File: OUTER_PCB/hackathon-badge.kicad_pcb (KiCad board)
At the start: 2 copper layers, 97.8 x 87.5 mm, 19 parts

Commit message: finished the outer board
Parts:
- removed the D1 at (154.5, 84.4)
- removed the D10 at (153.5, 128.4)
- removed D15: WS2812B-2020, LED_SMD:LED_WS2812B-2020_PLCC4_2.0x2.0mm
- removed the D5 at (175.7, 103.1)
- added TP1: TestPoint, TestPoint:TestPoint_Pad_4.0x4.0mm, B.Cu at (131.0, 106.0)
- added TP2: TestPoint, TestPoint:TestPoint_Pad_4.0x4.0mm, B.Cu at (177.0, 105.5)
- added TP3: TestPoint, TestPoint:TestPoint_Pad_4.0x4.0mm, B.Cu at (154.0, 84.0)
- added TP4: TestPoint, TestPoint:TestPoint_Pad_4.0x4.0mm, B.Cu at (154.0, 130.0)
- moved G*** 12.5 mm to (153.9, 118.5)
- moved D12 3.64 mm to (134.1, 98.5), turned to -110 degrees
- moved D11 1.37 mm to (133.0, 110.9), turned to -80 degrees
- moved D13 0.93 mm to (140.1, 90.2), turned to -140 degrees
- moved D4 0.87 mm to (174.8, 111.2), turned to 80 degrees
- moved D3 0.85 mm to (172.6, 96.4), turned to 120 degrees
- moved D14 0.84 mm to (146.7, 86.4), turned to -160 degrees
- moved D2 0.83 mm to (167.9, 90.5), turned to 140 degrees
- moved D1 0.80 mm to (161.7, 86.7), turned to 160 degrees
- moved D9 0.69 mm to (139.3, 122.3), turned to -40 degrees
- moved D7 0.60 mm to (160.5, 127.0), turned to 20 degrees
- moved D5 0.58 mm to (172.2, 117.8), turned to 60 degrees
- moved D10 0.55 mm to (135.2, 116.9), turned to -60 degrees
- moved D6 0.54 mm to (167.3, 123.3), turned to 40 degrees
- moved D8 0.45 mm to (146.0, 126.5), turned to -20 degrees
- renumbered D2 to D1, D13 to D10, D14 to D11, D16 to D12, D17 to D13, D18 to D14, D3 to D2, D4 to D3, D6 to D4, D7 to D5, D8 to D6, D9 to D7, D11 to D8, D12 to D9
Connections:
- D1 pad 3: Net-(D1-DOUT) (its old number) -> /LED_DIN
- D11 pad 1: Net-(D14-DOUT) -> Net-(D11-DOUT)
- D12 pad 3: Net-(D15-DOUT) -> Net-(D11-DOUT)
- D3 pad 1: Net-(D4-DOUT) (its old number) -> Net-(D3-DOUT)
- D4 pad 3: Net-(D5-DOUT) (its old number) -> Net-(D3-DOUT)
- D7 pad 1: Net-(D10-DIN) (its old number) -> Net-(D7-DOUT)
- D8 pad 3: Net-(D10-DOUT) (its old number) -> Net-(D7-DOUT)
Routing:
- net +5V: track 187.1 -> 145.0 mm, vias 0 -> 15
- net GND: track 0.00 -> 14.0 mm, vias 16 -> 15
- net Net-(D3-DOUT): track 0.00 -> 13.7 mm
- net Net-(D7-DOUT): track 0.00 -> 13.4 mm
- net Net-(D11-DOUT): track 0.00 -> 11.4 mm
- net Net-(D4-DOUT) (its old number): track 8.78 -> 0.00 mm
- net /LED_DIN: track 0.00 -> 7.85 mm
- net Net-(D5-DOUT) (its old number): track 7.23 -> 0.00 mm
- net Net-(D14-DOUT): track 7.23 -> 0.00 mm
- net Net-(D1-DOUT) (its old number): track 6.74 -> 0.00 mm
- net Net-(D10-DOUT) (its old number): track 6.74 -> 0.00 mm
- net Net-(D15-DOUT): track 6.41 -> 0.00 mm
- net Net-(D10-DIN) (its old number): track 5.75 -> 0.00 mm
- net Net-(D10-DOUT): track 7.91 -> 4.91 mm
- net Net-(D10-DIN): track 8.27 -> 5.51 mm
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
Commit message: finished second PCB
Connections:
- net +5V renamed +3.7V

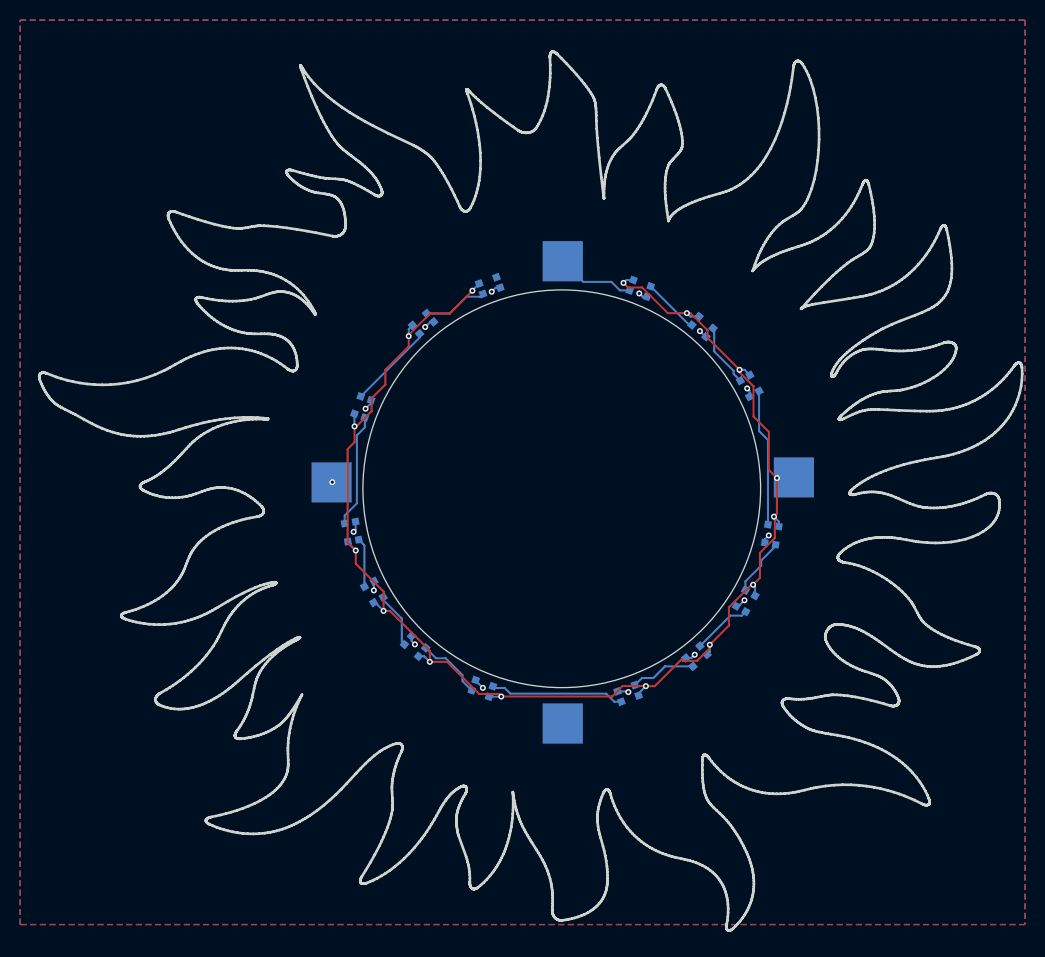
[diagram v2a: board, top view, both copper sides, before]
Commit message: some more art for the inner badge
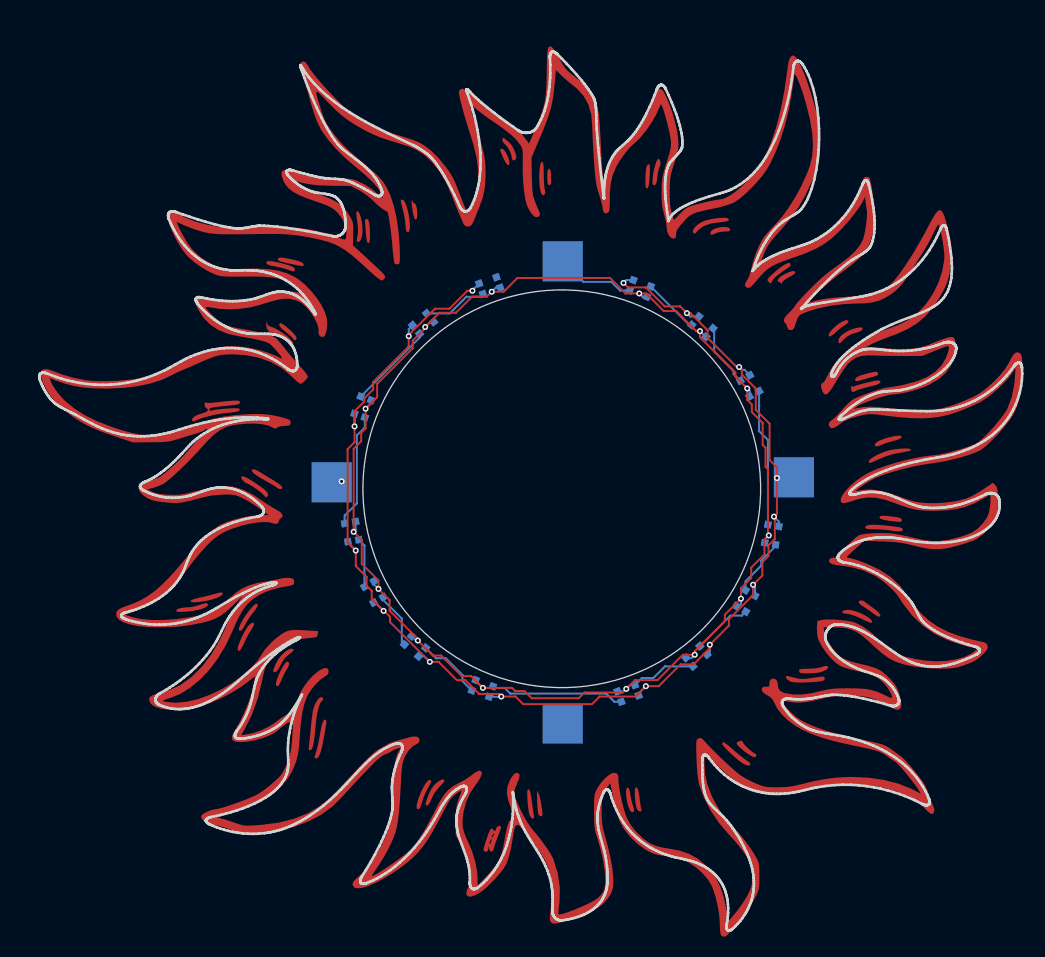
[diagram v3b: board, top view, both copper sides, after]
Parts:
- added G***: LOGO, LOGO, F.Cu at (150.9, 107.0)
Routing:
- net GND: track 14.0 -> 153.0 mm
- removed copper zone on B.Cu, net GND
- removed copper zone on F.Cu, net GND

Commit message: update
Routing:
- net GND: track 153.0 -> 161.1 mm, vias 15 -> 18
- net +3.7V: track 145.4 -> 145.9 mm, vias 15 -> 16
- net /LED_DIN: vias 0 -> 1
